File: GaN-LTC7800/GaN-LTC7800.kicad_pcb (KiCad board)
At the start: 2 copper layers, 40 parts, among them Q1 EPC2066, Q2 EPC2066, U1 LTC7800HUDC_PBF

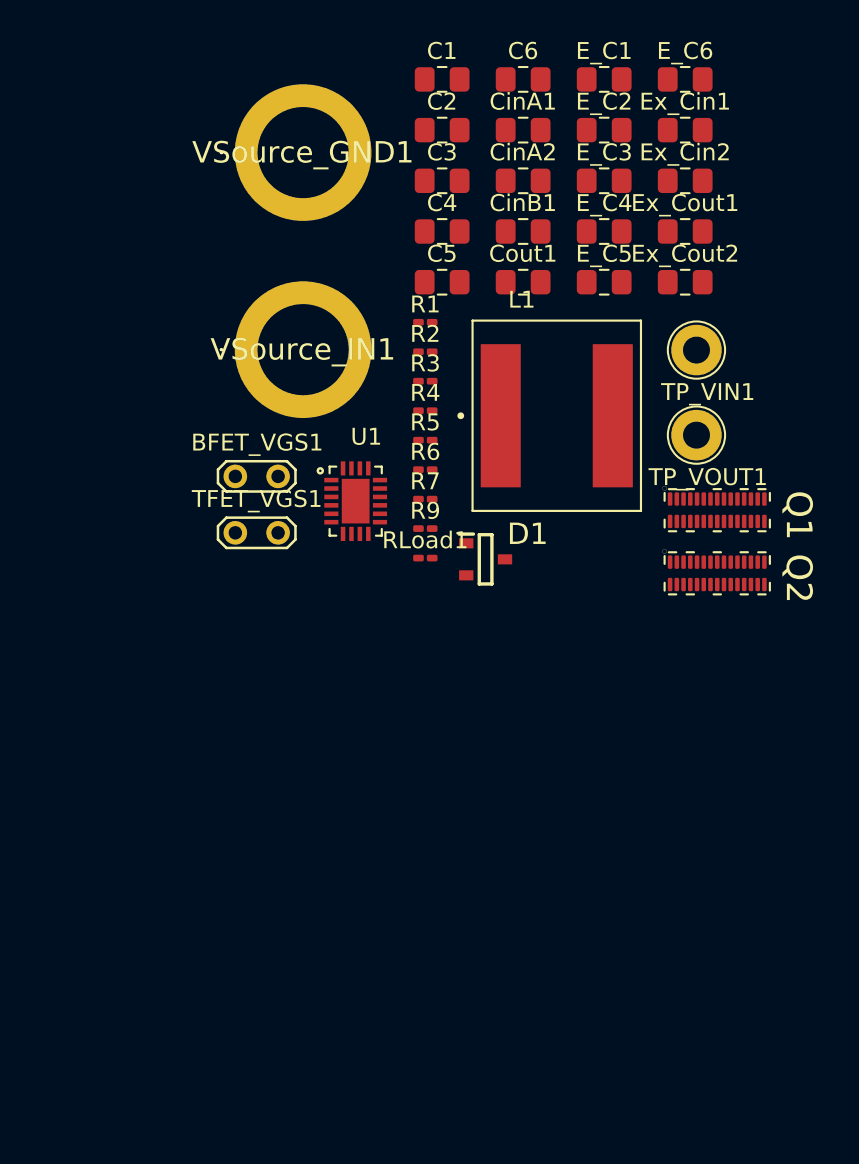
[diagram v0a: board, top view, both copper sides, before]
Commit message: Changed font size and names on PCB
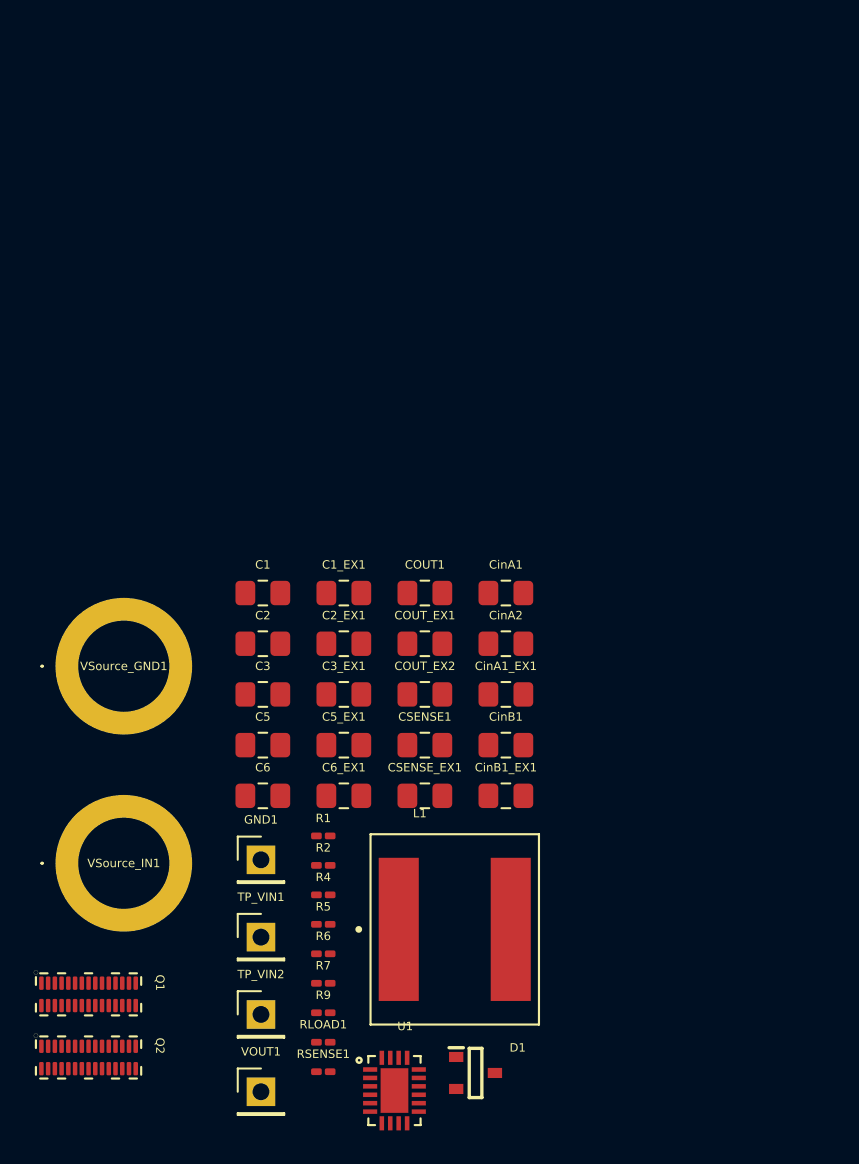
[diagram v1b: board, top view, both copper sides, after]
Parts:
- removed BFET_VGS1, TFET_VGS1: TestPoint_2Pole, TestPoint:TestPoint_2Pads_Pitch2.54mm_Drill0.8mm
- removed C4: 0.1uF, Capacitor_SMD:C_0805_2012Metric_Pad1.18x1.45mm_HandSolder
- removed Cout1: 100uF, Capacitor_SMD:C_0805_2012Metric_Pad1.18x1.45mm_HandSolder
- removed E_C1, E_C2, E_C3, E_C4, E_C5, E_C6, Ex_Cin1, Ex_Cin2, Ex_Cout1, Ex_Cout2: ~, Capacitor_SMD:C_0805_2012Metric_Pad1.18x1.45mm_HandSolder
- removed R3: 3mOhm, Resistor_SMD:R_0201_0603Metric_Pad0.64x0.40mm_HandSolder
- removed RLoad1: 5Ohm, Resistor_SMD:R_0201_0603Metric_Pad0.64x0.40mm_HandSolder
- removed TP_VOUT1: TestPoint, TestPoint:TestPoint_Loop_D2.60mm_Drill1.6mm_Beaded
- added C1_EX1: ~, Capacitor_SMD:C_0805_2012Metric_Pad1.18x1.45mm_HandSolder, F.Cu at (94.0, 109.5)
- added C2_EX1: ~, Capacitor_SMD:C_0805_2012Metric_Pad1.18x1.45mm_HandSolder, F.Cu at (94.0, 112.5)
- added C3_EX1: ~, Capacitor_SMD:C_0805_2012Metric_Pad1.18x1.45mm_HandSolder, F.Cu at (94.0, 115.5)
- added C5_EX1: ~, Capacitor_SMD:C_0805_2012Metric_Pad1.18x1.45mm_HandSolder, F.Cu at (94.0, 118.5)
- added C6_EX1: ~, Capacitor_SMD:C_0805_2012Metric_Pad1.18x1.45mm_HandSolder, F.Cu at (94.0, 121.5)
- added COUT1: 100uF, Capacitor_SMD:C_0805_2012Metric_Pad1.18x1.45mm_HandSolder, F.Cu at (98.8, 109.5)
- added COUT_EX1: ~, Capacitor_SMD:C_0805_2012Metric_Pad1.18x1.45mm_HandSolder, F.Cu at (98.8, 112.5)
- added COUT_EX2: ~, Capacitor_SMD:C_0805_2012Metric_Pad1.18x1.45mm_HandSolder, F.Cu at (98.8, 115.5)
- added CSENSE1: 0.1uF, Capacitor_SMD:C_0805_2012Metric_Pad1.18x1.45mm_HandSolder, F.Cu at (98.8, 118.5)
- added CSENSE_EX1: ~, Capacitor_SMD:C_0805_2012Metric_Pad1.18x1.45mm_HandSolder, F.Cu at (98.8, 121.5)
- added CinA1_EX1: ~, Capacitor_SMD:C_0805_2012Metric_Pad1.18x1.45mm_HandSolder, F.Cu at (103.7, 115.5)
- added CinB1_EX1: ~, Capacitor_SMD:C_0805_2012Metric_Pad1.18x1.45mm_HandSolder, F.Cu at (103.7, 121.5)
- added GND1: ~, Connector_PinHeader_2.54mm:PinHeader_1x01_P2.54mm_Vertical, F.Cu at (89.1, 125.3)
- added RLOAD1: 5Ohm, Resistor_SMD:R_0201_0603Metric_Pad0.64x0.40mm_HandSolder, F.Cu at (92.8, 136.2)
- added RSENSE1: 3mOhm, Resistor_SMD:R_0201_0603Metric_Pad0.64x0.40mm_HandSolder, F.Cu at (92.8, 137.9)
- added TP_VIN2: ~, Connector_PinHeader_2.54mm:PinHeader_1x01_P2.54mm_Vertical, F.Cu at (89.1, 134.5)
- added VOUT1: ~, Connector_PinHeader_2.54mm:PinHeader_1x01_P2.54mm_Vertical, F.Cu at (89.1, 139.1)
- TP_VIN1: value TestPoint -> ~; footprint TestPoint:TestPoint_Loop_D2.60mm_Drill1.6mm_Beaded -> Connector_PinHeader_2.54mm:PinHeader_1x01_P2.54mm_Vertical
- moved Q2 47.1 mm to (78.9, 137.1)
- moved Q1 47.1 mm to (78.9, 133.3)
- moved C6 45.3 mm to (89.2, 121.5)
- moved TP_VIN1 43.4 mm to (89.1, 129.9)
- moved U1 35.1 mm to (97.0, 139.0)
- moved C1 32.3 mm to (89.2, 109.5)
- moved C2 32.3 mm to (89.2, 112.5)
- moved C3 32.3 mm to (89.2, 115.5)
- moved VSource_IN1 32.3 mm to (81.0, 125.5)
- moved VSource_GND1 32.3 mm to (81.0, 113.8)
- moved R1 31.1 mm to (92.8, 123.9)
- moved R2 31.1 mm to (92.8, 125.7)
- moved L1 31.1 mm to (100.6, 129.5)
- moved CinB1 30.5 mm to (103.7, 118.5)
- moved D1 30.5 mm to (101.8, 138.0)
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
